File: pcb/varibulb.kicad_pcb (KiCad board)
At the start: 2 copper layers, 161.8 x 85.6 mm, 42 parts, among them IC1 ATTINY2313A-S, P1 MAINS LIVE, P2 BOARD, P3 BOARD, P4 RESET, P5 MAINS GROUND, P6 ISP, P7 COMM, SW1 ENCODER, U1 TRIAC, U2 LM2931AZ-3.3/5.0, X1 10MHz

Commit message: finish pcb
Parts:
- removed R10, R11: 10k, Resistors_SMD:R_0805
- added R4: 10Ω, Resistors_SMD:R_0805, B.Cu at (187.6, 78.1)
- R9: value 10k -> 100Ω
- moved C2 49.3 mm to (162.9, 79.4)
- moved C9 44.9 mm to (168.0, 92.1), turned to 180 degrees
- moved C10 44.5 mm to (167.6, 74.3), turned to 180 degrees
- moved R13 43.5 mm to (167.6, 71.8), turned to 180 degrees
- moved C8 42.9 mm to (168.0, 87.0), turned to 180 degrees
- moved C4 42.7 mm to (167.3, 79.4), turned to 180 degrees
- moved C11 38.0 mm to (193.4, 76.2), turned to 90 degrees
- moved R9 28.8 mm to (181.0, 87.3), turned to 180 degrees
- moved D7 20.0 mm to (162.2, 89.5), turned to 90 degrees
- moved P4 7.96 mm to (185.1, 82.2)
- moved X1 5.75 mm to (165.1, 81.9), turned to 0 degrees
- moved R7 3.00 mm to (187.6, 89.5)
- moved IC1 0.95 mm to (177.8, 74.6)
- moved R8 0.64 mm to (175.9, 93.3)
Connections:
- IC1 pad 15: /PHASE -> Net-(IC1-Pad15)
- IC1 pad 6: Net-(IC1-Pad2) -> Net-(IC1-Pad6)
- R9 pad 1: VCC -> Net-(IC1-Pad2)
- R9 pad 2: Net-(C8-Pad1) -> Net-(IC1-Pad6)
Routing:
- net GND: track 0.00 -> 154.2 mm
- net Net-(IC1-Pad15): track 0.00 -> 14.2 mm
- net /PHASE: track 16.2 -> 3.44 mm
- net Net-(IC1-Pad6): track 0.00 -> 10.3 mm
- net Net-(IC1-Pad2): track 34.1 -> 25.1 mm
- net Net-(D7-Pad1): track 7.46 -> 16.2 mm
- net Net-(IC1-Pad13): track 5.22 -> 13.7 mm
- net Net-(C2-Pad1): track 18.3 -> 25.6 mm
- net Net-(C10-Pad1): track 28.9 -> 33.0 mm
- net Net-(C4-Pad1): track 14.3 -> 16.4 mm
- net Net-(IC1-Pad1): track 15.8 -> 13.9 mm
- net VCC: track 42.0 -> 43.7 mm
- net Net-(IC1-Pad7): track 11.5 -> 13.1 mm
- net /SENSE: track 20.6 -> 21.7 mm
- net Net-(IC1-Pad3): track 29.8 -> 30.8 mm
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
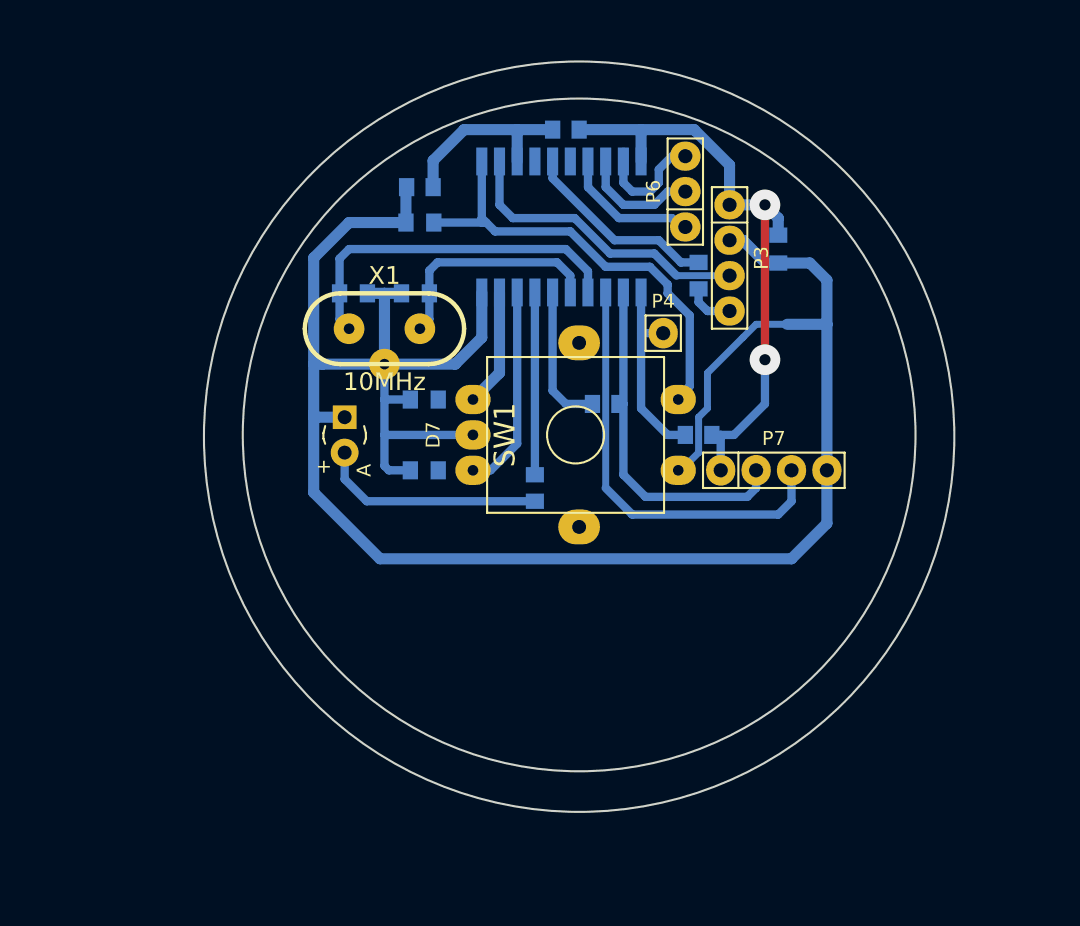
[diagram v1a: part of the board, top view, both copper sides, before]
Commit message: add filled zone
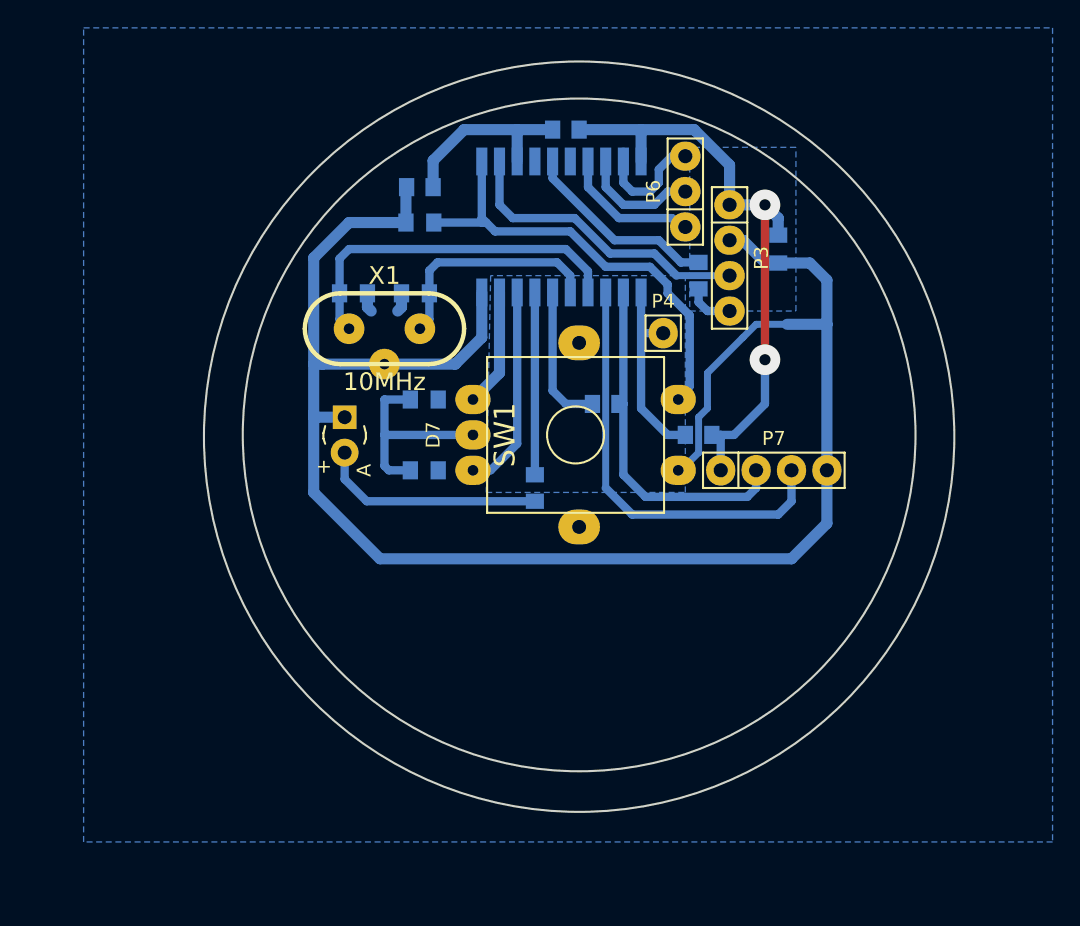
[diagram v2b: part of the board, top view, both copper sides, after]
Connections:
- SW1 pad : (no net) -> GND
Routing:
- net GND: track 154.2 -> 146.9 mm
- added copper zone on B.Cu, net GND

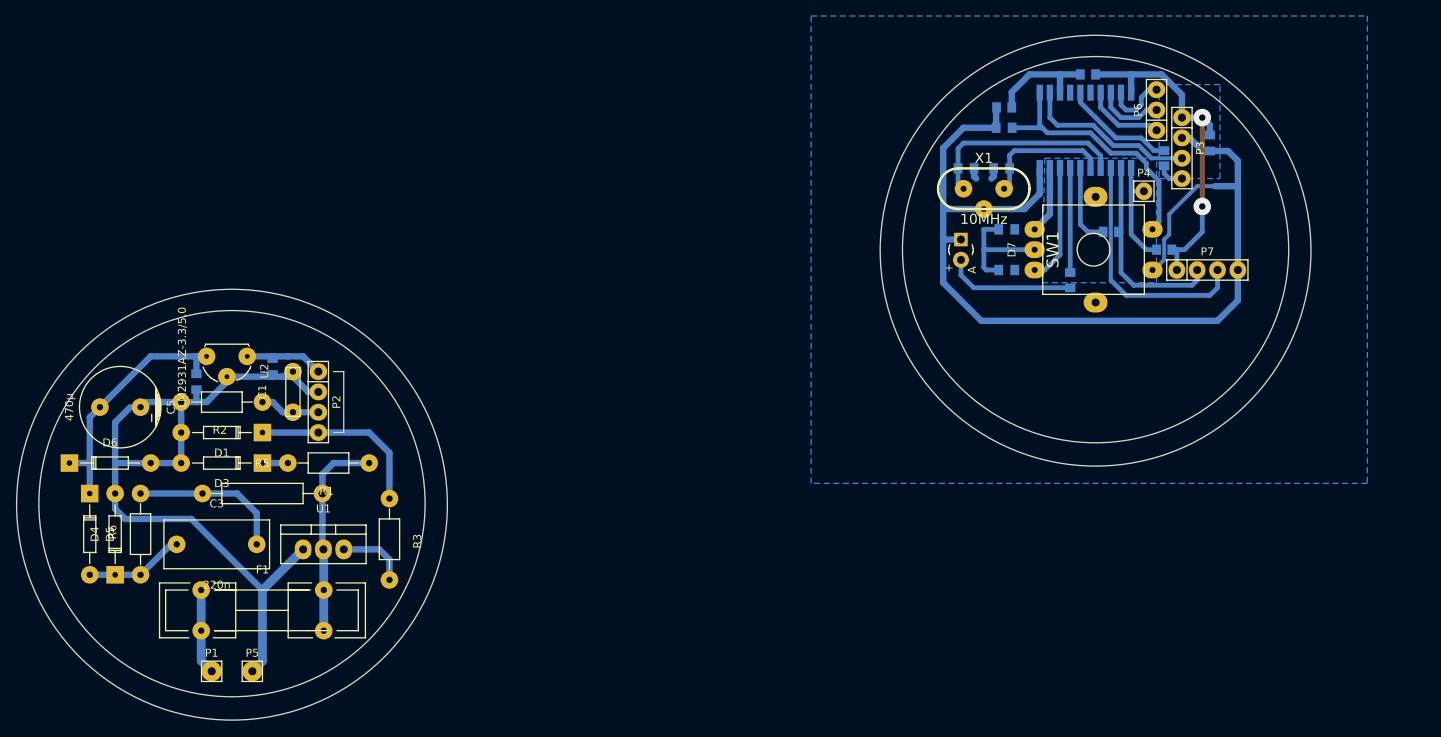
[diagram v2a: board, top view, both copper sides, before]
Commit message: remove the filled zone
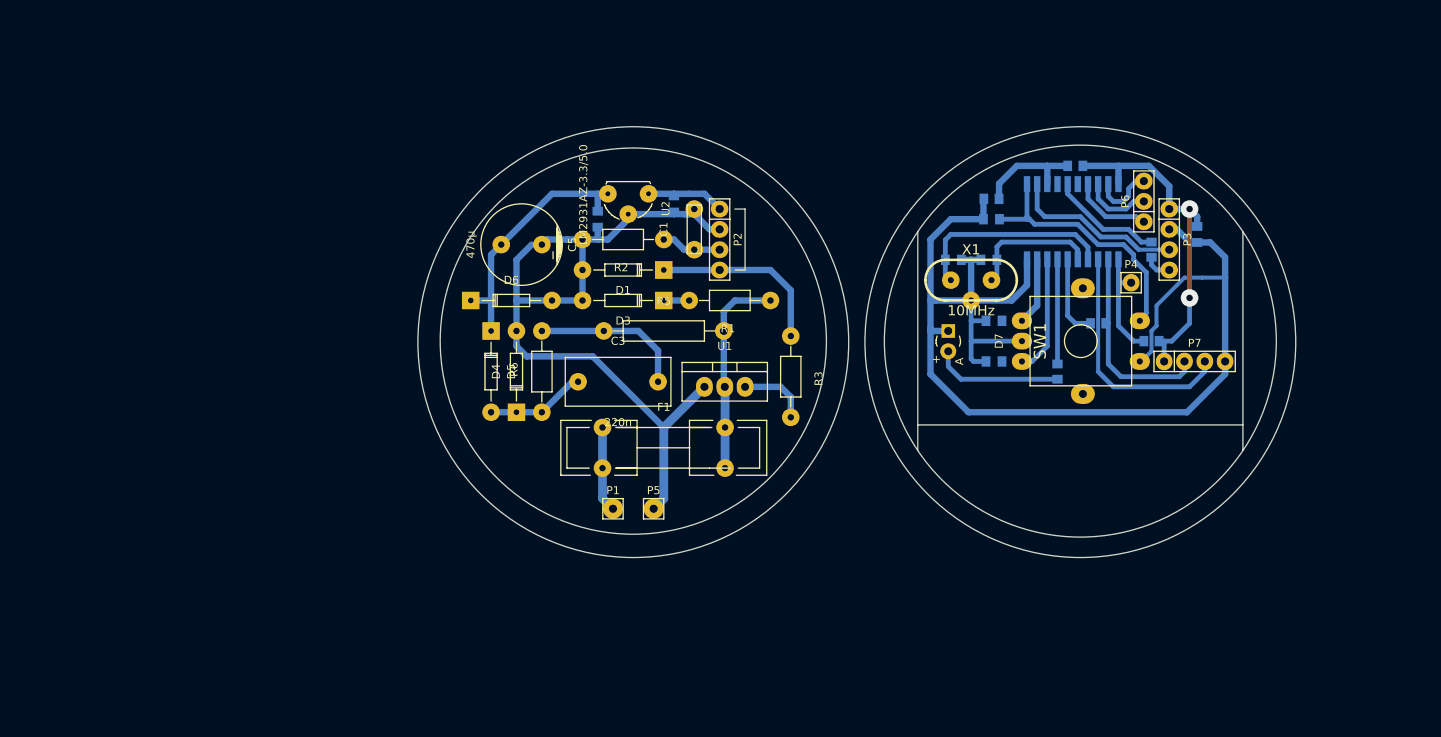
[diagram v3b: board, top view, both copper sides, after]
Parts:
- moved C1 54.1 mm to (128.9, 87.0)
- moved C6 54.1 mm to (116.8, 85.7)
- moved D1 54.1 mm to (120.0, 92.1)
- moved D3 54.1 mm to (120.0, 95.9)
- moved D4 54.1 mm to (106.7, 104.8)
- moved P1 54.1 mm to (118.7, 121.9)
- moved P2 54.1 mm to (132.1, 88.3)
- moved P5 54.1 mm to (123.8, 121.9)
- moved R2 54.1 mm to (120.0, 88.3)
- moved R6 54.1 mm to (109.9, 104.8)
- moved U1 54.1 mm to (132.7, 106.7)
- moved U2 54.1 mm to (120.7, 82.5)
- moved C5 54.1 mm to (107.3, 88.9)
- moved C7 54.1 mm to (126.4, 83.8)
- moved D6 54.1 mm to (106.0, 95.9)
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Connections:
- SW1 pad : GND -> (no net)
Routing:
- net GND: track 146.9 -> 152.5 mm
- net Net-(IC1-Pad3): track 30.8 -> 30.2 mm
- removed copper zone on B.Cu, net GND
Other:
- board size 161.8 x 85.6 mm -> 109.7 x 53.8 mm

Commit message: center edge outlines properly
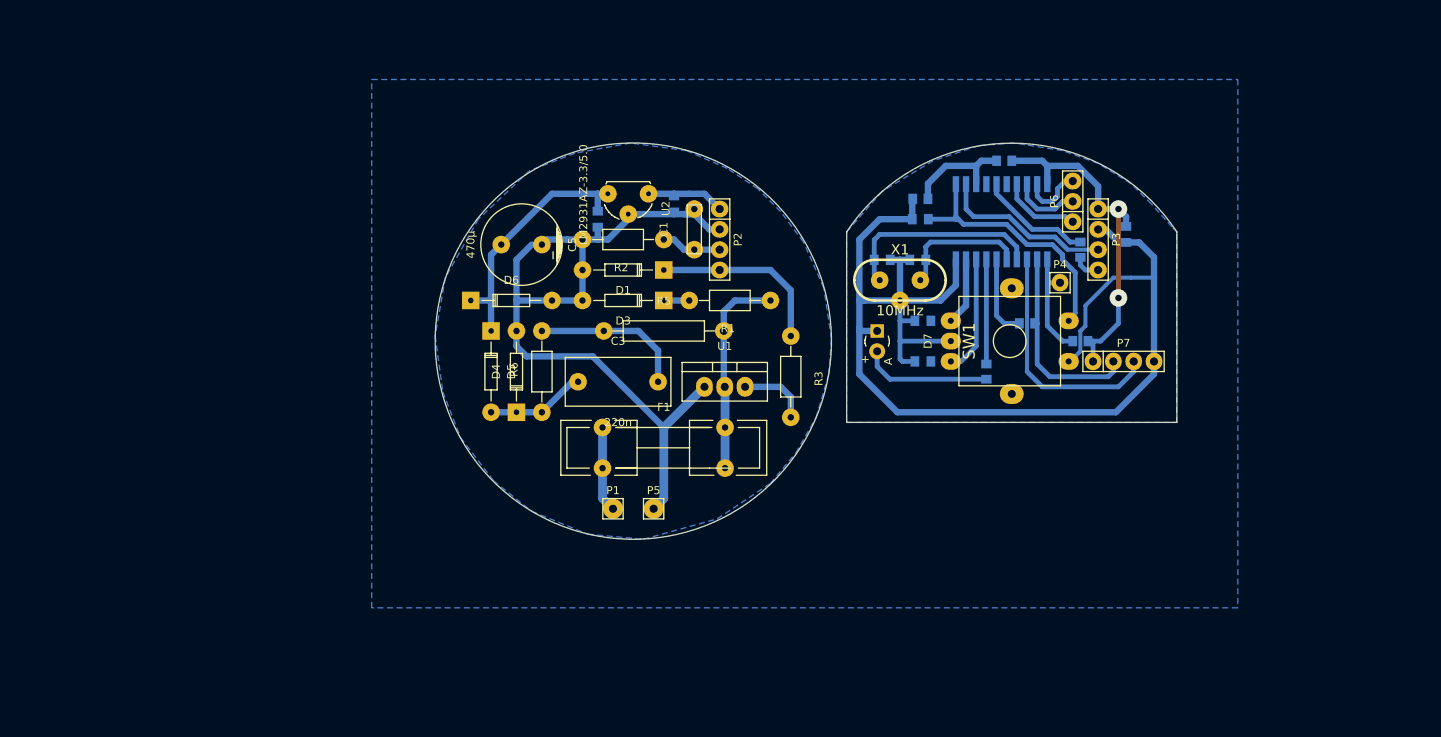
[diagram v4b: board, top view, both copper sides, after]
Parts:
- moved R12 8.91 mm to (167.6, 78.4)
- moved C10 8.89 mm to (157.2, 85.7)
- moved C11 8.89 mm to (182.9, 87.6)
- moved C4 8.89 mm to (156.8, 90.8)
- moved C8 8.89 mm to (157.5, 98.4)
- moved C9 8.89 mm to (157.5, 103.5)
- moved D7 8.89 mm to (151.8, 101.0)
- moved IC1 8.89 mm to (167.3, 86.0)
- moved P3 8.89 mm to (179.4, 88.3)
- moved R13 8.89 mm to (157.2, 83.2)
- moved R4 8.89 mm to (177.2, 89.5)
- moved R7 8.89 mm to (177.2, 101.0)
- moved R8 8.89 mm to (165.4, 104.8)
- moved C2 8.89 mm to (152.4, 90.8)
- moved P4 8.89 mm to (174.6, 93.7)
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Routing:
- added copper zone on B.Cu, net (none)
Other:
- board size 109.7 x 53.8 mm -> 92.7 x 49.5 mm

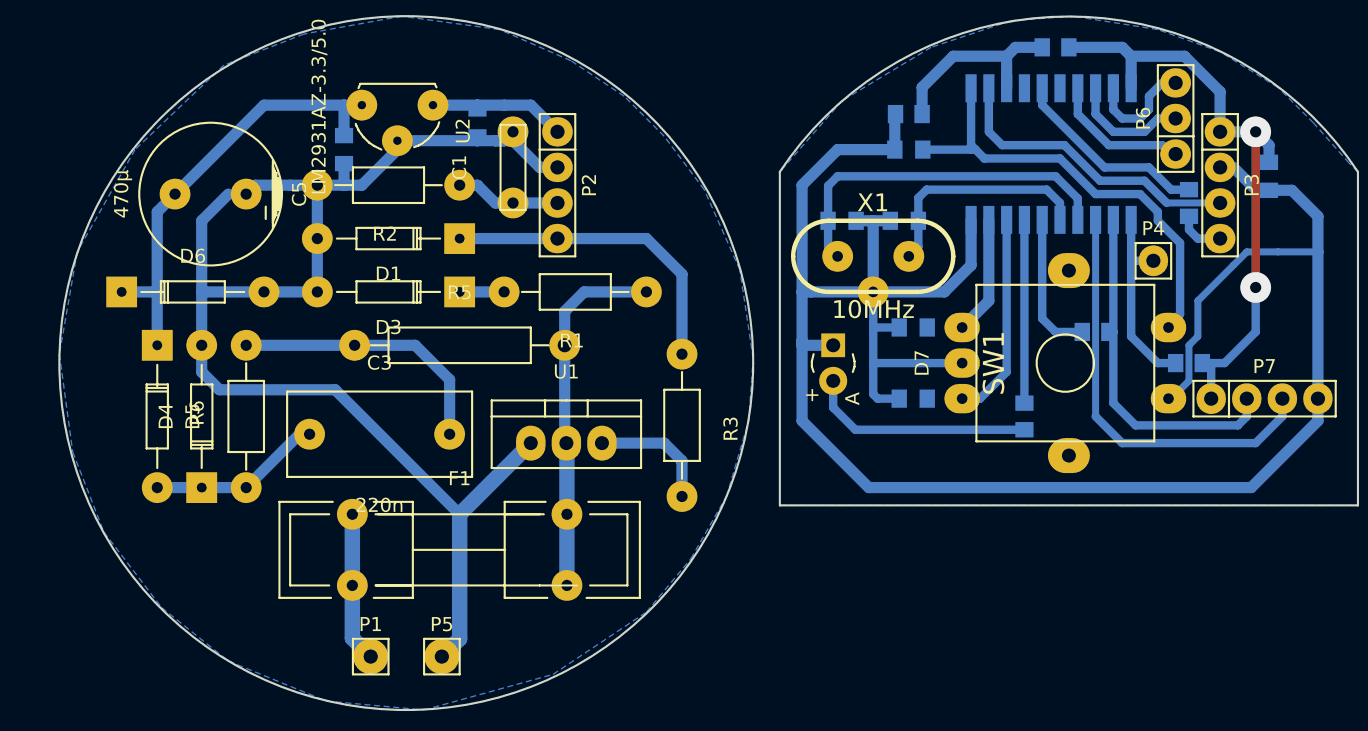
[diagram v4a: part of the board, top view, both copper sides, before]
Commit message: bigger capacitors
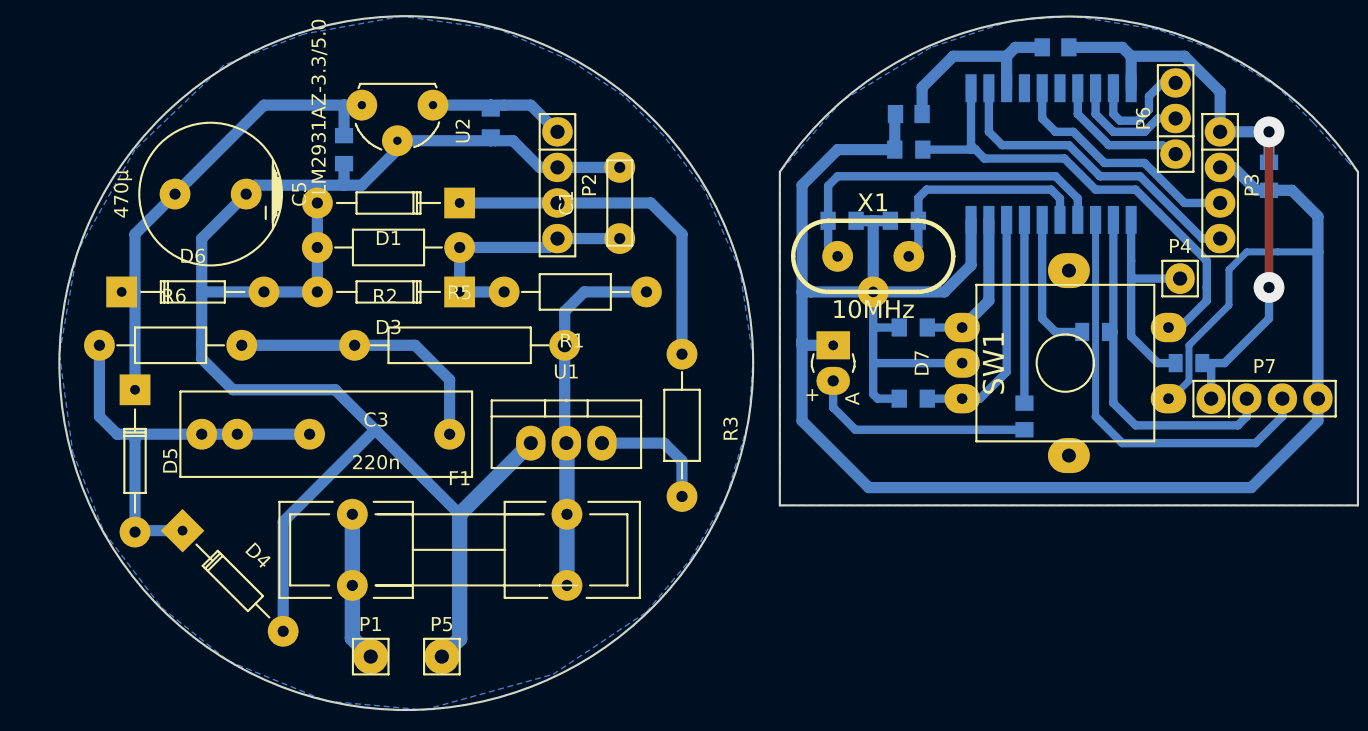
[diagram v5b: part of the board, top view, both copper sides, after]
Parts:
- removed R9: 100Ω, Resistors_SMD:R_0805
- C3: footprint Capacitors_ThroughHole:Capacitor13x6x12mmRM10 -> multi_capacitor:Capacitor13x6x12mmRM10
- R4: value 10Ω -> 100Ω
- moved D4 12.0 mm to (108.9, 116.5), turned to 135 degrees
- moved R4 11.4 mm to (170.5, 98.7), turned to 180 degrees
- moved C1 8.03 mm to (136.5, 89.5)
- moved R6 7.41 mm to (104.5, 99.7), turned to 0 degrees
- moved R2 4.44 mm to (120.0, 92.7)
- moved D5 3.55 mm to (101.9, 108.0)
- moved D1 2.54 mm to (120.0, 89.5)
- moved P4 2.29 mm to (176.5, 94.9)
- moved C7 0.95 mm to (127.3, 83.8)
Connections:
- IC1 pad 15: Net-(IC1-Pad15) -> /PHASE
- P2 pad 3: Net-(C1-Pad1) -> Net-(D1-Pad2)
- P2 pad 4: Net-(D1-Pad2) -> Net-(C1-Pad1)
- P3 pad 3: /SENSE -> /PHASE
- P3 pad 4: /PHASE -> /SENSE
- R4 pad 1: /PHASE -> Net-(IC1-Pad2)
- R4 pad 2: Net-(IC1-Pad15) -> Net-(IC1-Pad6)
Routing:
- net GNDREF: track 97.5 -> 118.2 mm
- net Net-(C3-Pad1): track 12.5 -> 32.4 mm
- net Net-(IC1-Pad15): track 14.2 -> 0.00 mm
- net /PHASE: track 3.44 -> 17.4 mm
- net Net-(C1-Pad1): track 11.3 -> 18.0 mm
- net Net-(C5-Pad1): track 32.0 -> 34.9 mm
- net Net-(D1-Pad2): track 22.6 -> 25.4 mm
- net Net-(C9-Pad1): track 14.8 -> 17.3 mm
- net Net-(C8-Pad1): track 8.47 -> 11.0 mm
- net Net-(C10-Pad1): track 33.0 -> 35.2 mm
- net Net-(IC1-Pad1): track 13.9 -> 15.8 mm
- net /SENSE: track 21.7 -> 22.8 mm
- net VCC: track 43.9 -> 44.9 mm

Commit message: make PCB prints
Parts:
- added MountingHole_3mm: VAL**, Mounting_Holes:MountingHole_3mm, F.Cu at (136.5, 99.4)
- added MountingHole_3mm: VAL**, Mounting_Holes:MountingHole_3mm, F.Cu at (183.8, 99.4)
- moved R5 1.27 mm to (123.8, 99.7)
- moved R1 0.64 mm to (133.3, 95.2)
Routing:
- net GND: track 152.5 -> 158.7 mm
- net Net-(F1-Pad2): track 26.3 -> 28.5 mm
- net VCC: track 44.9 -> 44.3 mm
